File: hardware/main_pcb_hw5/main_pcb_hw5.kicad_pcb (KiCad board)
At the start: 2 copper layers, 100 x 100 mm, 27 parts, among them J1 MEGA TOP, J10 GBA_Slot, J2 MEGA BOTTOM, J3 CART SLOT TOP ROW, J4 CART SLOT BOTTOM ROW, J5 MEGA SIDE, J6 5V USB, J7 Conn_01x07, J8 EXP2, J9 EXP1, M2_1 Screw_Terminal_01x01, M2_2 Screw_Terminal_01x01, M2_3 Screw_Terminal_01x01, M2_4 Screw_Terminal_01x01, M2_5 Screw_Terminal_01x01, M2_6 Screw_Terminal_01x01, M2_7 Screw_Terminal_01x01, M2_8 Screw_Terminal_01x01, M2_9 Screw_Terminal_01x01, SW1 VOLTAGE, SW2 POWER

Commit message: relink footprints to symbols
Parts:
- J10: footprint !sanni:GBA-SLOT-B -> !OSCR:GBA_Slot
- JP1: value powered by VCC -> J1
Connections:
- J10 pad SHIELD_3: GND -> (no net)
- J10 pad SHIELD_4: GND -> (no net)
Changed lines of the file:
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@@
     )
   )
-  (footprint "!sanni:GBA-SLOT-B" (layer "F.Cu")
+  (footprint "!OSCR:GBA_Slot" (layer "F.Cu")
     (at 150 68.5 90)
     (property "Sheetfile" "main_pcb_hw5.kicad_sch")
@@
       (effects (font (size 1.2065 1.2065) (thickness 0.1016)) (justify left bottom))
     )
-    (fp_line (start -2.5 25.5) (end -2.5 28) (layer "F.Fab") (width 0.1))
+    (fp_line (start -2.5 28) (end -2.5 28.5) (layer "F.Fab") (width 0.1))
+    (fp_line (start 15 -28) (end 15 -25.5) (layer "F.Fab") (width 0.1))
+    (fp_line (start 15 28) (end 15 28.5) (layer "F.Fab") (width 0.1))
+    (fp_line (start 15 28.5) (end -2.5 28.5) (layer "F.Fab") (width 0.1))
+    (fp_line (start 15 28) (end 15 25.5) (layer "F.Fab") (width 0.1))
     (fp_line (start -4 25.5) (end -2.5 25.5) (layer "F.Fab") (width 0.1))
-    (fp_line (start 15 -28) (end 15 -25.5) (layer "F.Fab") (width 0.1))
-    (fp_line (start -2.5 28) (end -2.5 28.5) (layer "F.Fab") (width 0.1))
-    (fp_line (start 15 -25.5) (end 15 25.5) (layer "F.Fab") (width 0.1))
-    (fp_line (start -4 -25.5) (end -4 25.5) (layer "F.Fab") (width 0.1))
-    (fp_line (start 15 28) (end 15 28.5) (layer "F.Fab") (width 0.1))
-    (fp_line (start 15 28) (end 15 25.5) (layer "F.Fab") (width 0.1))
     (fp_line (start -2.5 -28.5) (end -2.5 -28) (layer "F.Fab") (width 0.1))
     (fp_line (start -2.5 -25.5) (end -4 -25.5) (layer "F.Fab") (width 0.1))
+    (fp_line (start -2.5 25.5) (end -2.5 28) (layer "F.Fab") (width 0.1))
+    (fp_line (start 15 -28.5) (end -2.5 -28.5) (layer "F.Fab") (width 0.1))
+    (fp_line (start -2.5 -25.5) (end -2.5 -28) (layer "F.Fab") (width 0.1))
+    (fp_line (start 15 -25.5) (end 15 25.5) (layer "F.Fab") (width 0.1))
     (fp_line (start 15 -28) (end 15 -28.5) (layer "F.Fab") (width 0.1))
-    (fp_line (start -2.5 -25.5) (end -2.5 -28) (layer "F.Fab") (width 0.1))
-    (fp_line (start 15 28.5) (end -2.5 28.5) (layer "F.Fab") (width 0.1))
-    (fp_line (start 15 -28.5) (end -2.5 -28.5) (layer "F.Fab") (width 0.1))
+    (fp_line (start -4 -25.5) (end -4 25.5) (layer "F.Fab") (width 0.1))
+    (pad "" np_thru_hole circle locked (at 3.5 13 90) (size 2.2 2.2) (drill 2.2) (layers *.Cu *.Mask))
     (pad "" np_thru_hole circle locked (at 3.5 -13 90) (size 2.2 2.2) (drill 2.2) (layers *.Cu *.Mask))
-    (pad "" np_thru_hole circle locked (at 3.5 13 90) (size 2.2 2.2) (drill 2.2) (layers *.Cu *.Mask))
     (pad "1" smd rect locked (at -5 -23.25 270) (size 5 1) (layers "F.Cu" "F.Paste" "F.Mask")
       (net 36 "VCC") (pinfunction "VCC") (pintype "power_in") (solder_mask_margin 0.0508))
@@
       (net 37 "GND") (pinfunction "GND") (pintype "power_in") (solder_mask_margin 0.0508))
     (pad "SHIELD_3" smd rect locked (at 16.25 -13) (size 5.5 3.5) (layers "F.Cu" "F.Paste" "F.Mask")
-      (net 37 "GND") (solder_mask_margin 0.0508))
+      (solder_mask_margin 0.0508))
     (pad "SHIELD_4" smd rect locked (at 16.25 13) (size 5.5 3.5) (layers "F.Cu" "F.Paste" "F.Mask")
-      (net 37 "GND") (solder_mask_margin 0.0508))
+      (solder_mask_margin 0.0508))
   )
   (footprint "Connector_IDC:IDC-Header_2x05_P2.54mm_Vertical" (layer "F.Cu")
@@
       (effects (font (size 1 1) (thickness 0.15)) (justify mirror))
     )
-    (fp_text value "powered by VCC" (at 3.01 1.66 180 unlocked) (layer "B.SilkS") hide
+    (fp_text value "J1" (at 3.01 1.66 180 unlocked) (layer "B.SilkS") hide
       (effects (font (size 0.7 0.7) (thickness 0.15)) (justify left mirror))
     )
@@
     (effects (font (size 1 1) (thickness 0.15)) (justify mirror))
   )
+  (dimension (type orthogonal) (layer "Dwgs.User")
+    (pts (xy 100 148) (xy 200 148))
+    (height 11.398)
+    (orientation 0)
+    (gr_text "100.0000 mm" (at 150 158.248) (layer "Dwgs.User")
+      (effects (font (size 1 1) (thickness 0.15)))
+    )
+    (format (units 3) (units_format 1) (precision 4))
+    (style (thickness 0.15) (arrow_length 1.27) (text_position_mode 0) (extension_height 0.58642) (extension_offset 0.5) keep_text_aligned)
+  )
+  (dimension (type orthogonal) (layer "Dwgs.User")
+    (pts (xy 102 50) (xy 102 150))
+    (height -12.16)
+    (orientation 1)
+    (gr_text "100.0000 mm" (at 88.69 100 90) (layer "Dwgs.User")
+      (effects (font (size 1 1) (thickness 0.15)))
+    )
+    (format (units 3) (units_format 1) (precision 4))
+    (style (thickness 0.15) (arrow_length 1.27) (text_position_mode 0) (extension_height 0.58642) (extension_offset 0.5) keep_text_aligned)
+  )
+  (dimension (type orthogonal) (layer "Dwgs.User")
+    (pts (xy 193.98 104.255) (xy 198.044 81.395))
+    (height 24.13)
+    (orientation 1)
+    (gr_text "22.8600 mm" (at 216.96 92.825 90) (layer "Dwgs.User")
+      (effects (font (size 1 1) (thickness 0.15)))
+    )
+    (format (units 3) (units_format 1) (precision 4))
+    (style (thickness 0.15) (arrow_length 1.27) (text_position_mode 0) (extension_height 0.58642) (extension_offset 0.5) keep_text_aligned)
+  )
   (segment (start 168.6 81.395) (end 168.6 80.1447) (width 0.4) (layer "F.Cu") (net 1))

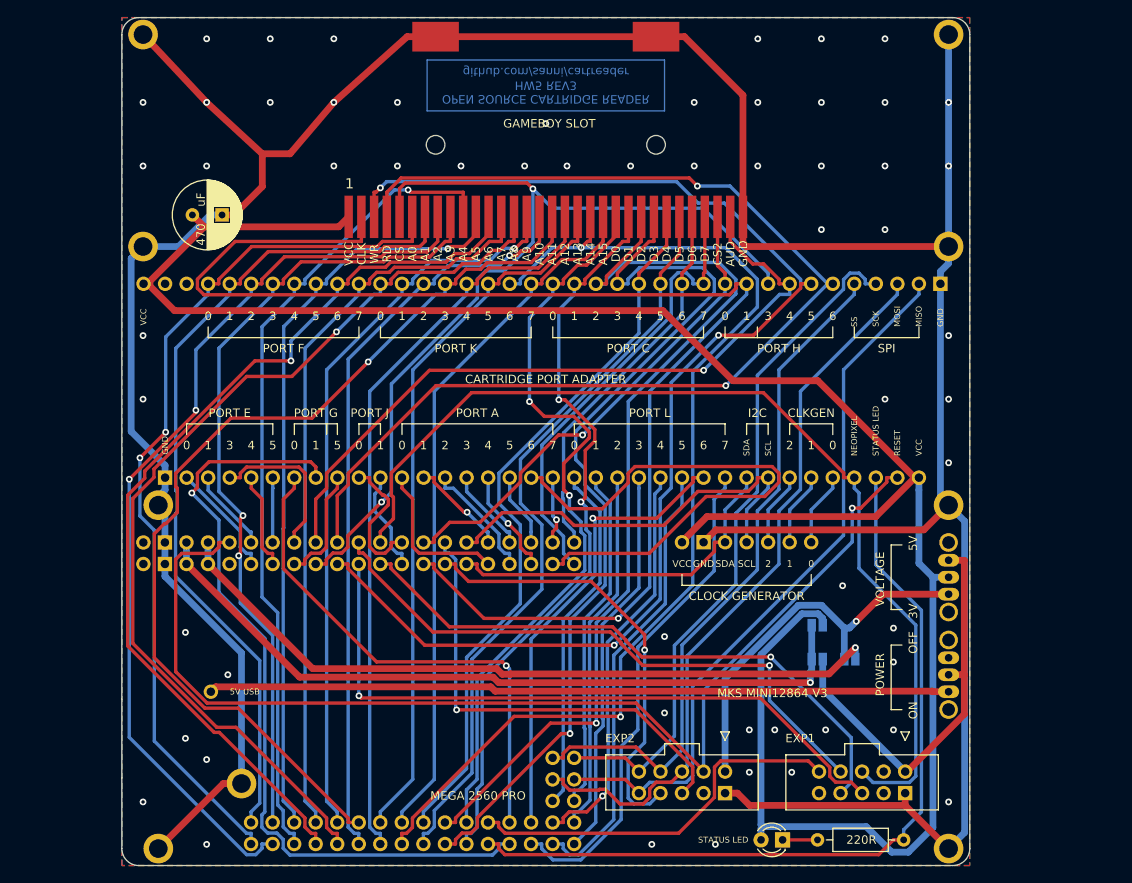
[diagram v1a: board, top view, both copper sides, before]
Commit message: remove gba slot from main pcb
GBA cart slot is removed to simplify and shrink the main PCB.
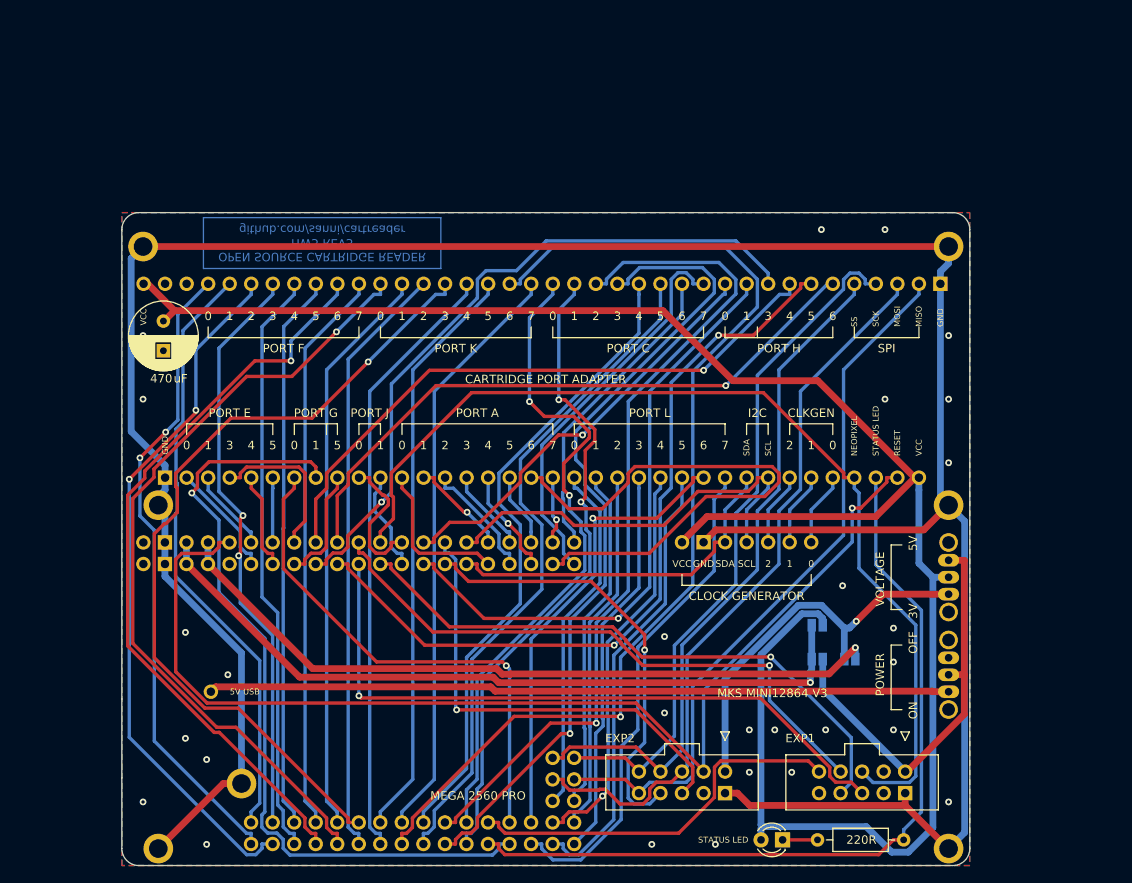
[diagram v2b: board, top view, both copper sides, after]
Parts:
- removed J10: GBA_Slot, !OSCR:GBA_Slot
- removed M2_1, M2_2: Screw_Terminal_01x01, MountingHole:MountingHole_2.2mm_M2_ISO7380_Pad
- moved C1 13.0 mm to (104.9, 85.8), turned to -90 degrees
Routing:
- net D16: track 162.7 -> 71.7 mm
- net GND: track 390.5 -> 312.5 mm, vias 58 -> 28
- net D9: track 135.9 -> 75.1 mm, vias 2 -> 1
- net D8: track 152.6 -> 92.3 mm, vias 3 -> 2
- net A0: track 104.5 -> 75.1 mm
- net D6: track 110.2 -> 81.8 mm, vias 2 -> 1
- net A1: track 99.2 -> 70.8 mm
- net A4: track 97.3 -> 69.5 mm, vias 1 -> 0
- net VCC: track 259.2 -> 231.8 mm
- net A2: track 110.2 -> 82.9 mm
- net A3: track 95.4 -> 69.2 mm
- net A5: track 89.3 -> 65.7 mm, vias 1 -> 0
- net A6: track 111.3 -> 88.6 mm
- net A7: track 88.7 -> 66.7 mm
- net A8: track 114.4 -> 93.4 mm
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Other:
- board size 100 x 100 mm -> 100 x 77 mm
- board text removed: "AUD"
- board text removed: "CLK"
- board text removed: "CS"
- board text removed: "CS2"
- board text removed: "GAMEBOY SLOT"
- board text removed: "RD"
- board text removed: "WR"

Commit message: Update Main PCB
Change basic design to a shield. Remove GBA Port. Add buck converters to main board.
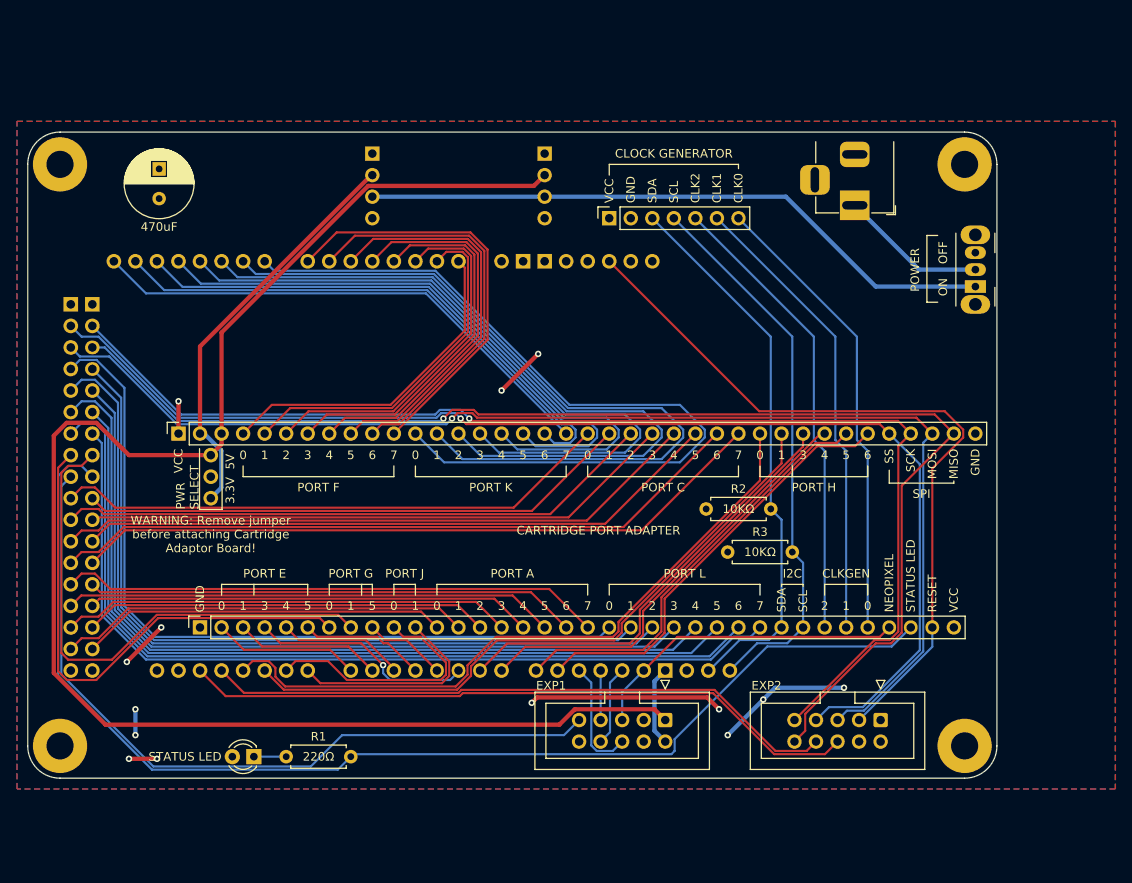
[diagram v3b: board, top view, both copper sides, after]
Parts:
- removed the J4 at (105.1, 104.3)
- removed the J7 at (166.1, 111.9)
- removed JP1: J1, Jumper:SolderJumper-2_P1.3mm_Open_Pad1.0x1.5mm
- removed JP2: Testpoints 1 2, Jumper:SolderJumper-2_P1.3mm_Open_Pad1.0x1.5mm
- removed JP3: Testpoints 3 4, Jumper:SolderJumper-2_P1.3mm_Open_Pad1.0x1.5mm
- removed M2_3, M2_4, M2_5, M2_6, M2_7, M2_8, M2_9: Screw_Terminal_01x01, MountingHole:MountingHole_2.2mm_M2_ISO7380_Pad
- removed the SW1 at (197.5, 118.0)
- added H1: MountingHole_Pad, MountingHole:MountingHole_3.2mm_M3_Pad, F.Cu at (92.7, 135.9)
- added H2: MountingHole_Pad, MountingHole:MountingHole_3.2mm_M3_Pad, F.Cu at (199.4, 135.9)
- added H3: MountingHole_Pad, MountingHole:MountingHole_3.2mm_M3_Pad, F.Cu at (199.4, 67.3)
- added H4: MountingHole_Pad, MountingHole:MountingHole_3.2mm_M3_Pad, F.Cu at (92.7, 67.3)
- added J3: 3.3V Buck (MPM3610), Connector_PinHeader_2.54mm:PinHeader_1x04_P2.54mm_Vertical, B.Cu at (129.5, 66.0)
- added J9: Power_Select, Connector_PinHeader_2.54mm:PinHeader_1x03_P2.54mm_Vertical, F.Cu at (110.5, 106.7)
- added R2: 10K, Resistor_THT:R_Axial_DIN0207_L6.3mm_D2.5mm_P7.62mm_Horizontal, F.Cu at (168.9, 108.0)
- added R3: 10K, Resistor_THT:R_Axial_DIN0207_L6.3mm_D2.5mm_P7.62mm_Horizontal, F.Cu at (171.4, 113.0)
- added XA1: Arduino_Mega2560_Shield, Arduino:Arduino_Mega2560_Shield, F.Cu at (190.5, 76.2)
- J1: value MEGA TOP -> Barrel_Jack(+12V); footprint Connector_PinSocket_2.54mm:PinSocket_2x21_P2.54mm_Vertical -> Connector_BarrelJack:BarrelJack_Horizontal
- J2: value MEGA BOTTOM -> 5V Buck (MPM3610); footprint Connector_PinSocket_2.54mm:PinSocket_2x16_P2.54mm_Vertical -> Connector_PinHeader_2.54mm:PinHeader_1x04_P2.54mm_Vertical; moved to B.Cu
- J5: value MEGA SIDE -> CART SLOT BOTTOM ROW; footprint Connector_PinSocket_2.54mm:PinSocket_2x03_P2.54mm_Vertical -> Connector_PinSocket_2.54mm:PinSocket_1x36_P2.54mm_Vertical
- J6: value 5V USB -> Conn_01x07; footprint Connector_PinHeader_2.54mm:PinHeader_1x01_P2.54mm_Vertical -> Connector_PinSocket_2.54mm:PinSocket_1x07_P2.54mm_Vertical
- R1: footprint Resistor_THT:R_Axial_DIN0207_L6.3mm_D2.5mm_P10.16mm_Horizontal -> Resistor_THT:R_Axial_DIN0207_L6.3mm_D2.5mm_P7.62mm_Horizontal
- moved J2 81.5 mm to (149.9, 66.0), turned to 180 degrees
- moved J6 73.0 mm to (157.5, 73.7), turned to 90 degrees
- moved R1 63.4 mm to (119.4, 137.2)
- moved D1 63.1 mm to (115.6, 137.2)
- moved J1 53.7 mm to (186.4, 72.1)
- moved SW1 47.9 mm to (200.7, 81.7)
- moved J5 46.3 mm to (109.2, 121.9), turned to 90 degrees
- moved J7 28.9 mm to (164.1, 132.8)
- moved J8 19.3 mm to (189.5, 132.8)
- moved J4 18.1 mm to (106.7, 99.1)
- moved C1 14.5 mm to (104.4, 71.3), turned to 90 degrees
- renumbered J3 to J4, J9 to J7, SW2 to SW1
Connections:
- J1 pad 1: D30 -> +VDC
- J1 pad 2: D31 -> GND
- J2 pad 1: D46 -> GND
- J2 pad 2: D47 -> +5V
- J2 pad 3: D44 -> VBUS
- J2 pad 4: D45 -> unconnected-(J2-Pin_4-Pad4)
- J4 pad 2: unconnected-(J3-Pad2) -> +3.3V
- J4 pad 3: unconnected-(J3-Pad3) -> +5V
- J4 pad 34: D53 -> SS
- J4 pad 35: D52 -> SCK
- J4 pad 36: D51 -> MOSI
- J4 pad 37: D50 -> MISO
- J5 pad 1: D49 -> GND
- J5 pad 2: D48 -> D0
- J5 pad 3: D51 -> D1
- J5 pad 4: D50 -> D5
- J5 pad 5: D53 -> D2
- J5 pad 6: D52 -> D3
- J6 pad 1: VBUS -> VCC
- J8 pad 1: +3V3 -> unconnected-(J8-Pin_1-Pad1)
- J8 pad 10: D50 -> MISO
- J8 pad 5: D51 -> MOSI
- J8 pad 7: D53 -> SS
- J8 pad 9: D52 -> SCK
- SW1 pad 2: +5V -> +VDC
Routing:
- net GND: track 312.5 -> 28.5 mm, vias 28 -> 5
- net VCC: track 231.8 -> 41.9 mm, vias 0 -> 9
- net MISO: track 0.00 -> 152.1 mm, vias 0 -> 1
- net MOSI: track 0.00 -> 146.5 mm, vias 0 -> 1
- net SS: track 0.00 -> 144.9 mm, vias 0 -> 1
- net SCK: track 0.00 -> 142.8 mm, vias 0 -> 1
- net +5V: track 48.9 -> 185.4 mm
- net VDDA: track 88.7 -> 0.00 mm, vias 1 -> 0
- net D51: track 87.1 -> 0.00 mm
- net +3.3VA: track 86.9 -> 0.00 mm, vias 1 -> 0
- net D50: track 84.6 -> 0.00 mm
- net D53: track 81.7 -> 0.00 mm
- net D52: track 81.3 -> 0.00 mm
- net D13: track 117.3 -> 38.0 mm
- net D10: track 80.3 -> 13.8 mm, vias 1 -> 0
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- added copper zone on B.Cu, net VCC
- removed copper zone on B.Cu, net GND
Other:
- board size 100 x 77 mm -> 114.3 x 76.2 mm
- board text added: "10KΩ"
- board text added: "220Ω"
- board text added: "3.3V"
- board text added: "3.3V 5V"
- board text added: "3.3V Buck Converter"
- board text added: "470uF"
- board text added: "5V Buck Converter"
- board text added: "OSCR SHIELD github.com/akreager/cartreader BASED ON OPEN SOURCE CARTRIDGE READER github.com/sanni/cartreader"
- board text added: "PWR SELECT"
- board text added: "Vin"
- board text added: "WARNING: Remove jumper before attaching Cartridge Adaptor Board!"
- board text removed: "220R"
- board text removed: "3V"
- board text removed: "3V3"
- board text removed: "470"
- board text removed: "5V USB"
- board text removed: "D20"
- board text removed: "D21"
- board text removed: "J1"
- board text removed: "J2"
- board text removed: "MEGA 2560 PRO"
- board text removed: "MKS MINI12864 V3"
- board text removed: "ON LCD"
- board text removed: "OPEN SOURCE CARTRIDGE READER HW5 REV3 github.com/sanni/cartreader"
- board text removed: "TP1"
- board text removed: "TP2"
- board text removed: "TP3"
- board text removed: "TP4"
- board text removed: "VOLTAGE"
- board text removed: "uF"
